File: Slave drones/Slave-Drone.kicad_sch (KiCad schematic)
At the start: 41 parts, among them J1 Conn_01x02, J2 Conn_01x02, J3 Conn_01x02, J4 Conn_01x02, J5 USB_C_Receptacle_USB2.0_16P, J6 Conn_01x02, SW1 SW_Push, SW2 SW_Push, U1 MPU6500, U2 QMC5883L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

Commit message: tried fixing error 3 - failed - use work around
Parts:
- U3: footprint ESP32-S3-MINI-1-N8:XCVR_ESP32-S3-MINI-1-N8 -> footprint-JLC:BULETM-SMD_ESP32-S3-MINI-1-N8
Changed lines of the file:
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@@
 			)
 		)
-		(property "Footprint" "ESP32-S3-MINI-1-N8:XCVR_ESP32-S3-MINI-1-N8"
+		(property "Footprint" "footprint-JLC:BULETM-SMD_ESP32-S3-MINI-1-N8"
 			(at 167.64 119.38 0)
 			(hide yes)

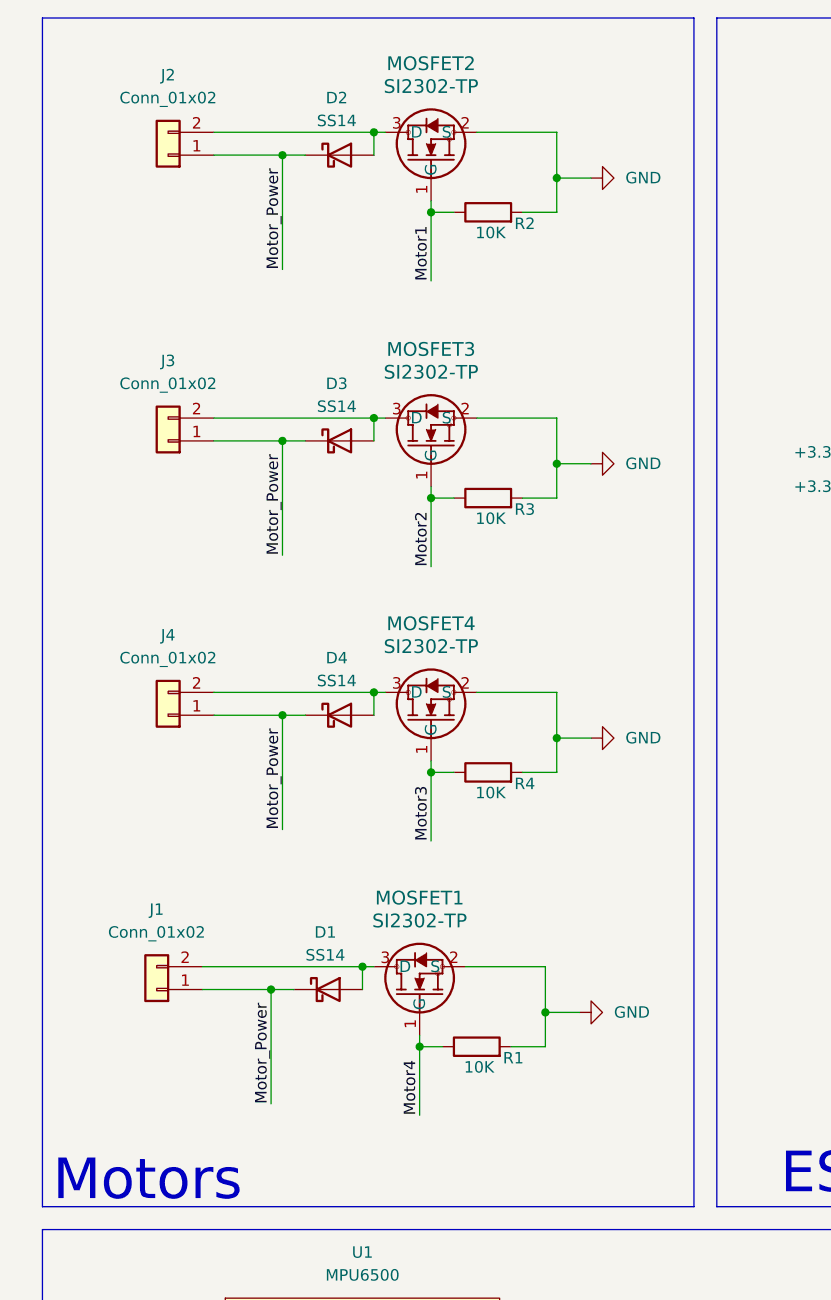
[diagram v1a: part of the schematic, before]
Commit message: corrected mosfet placement
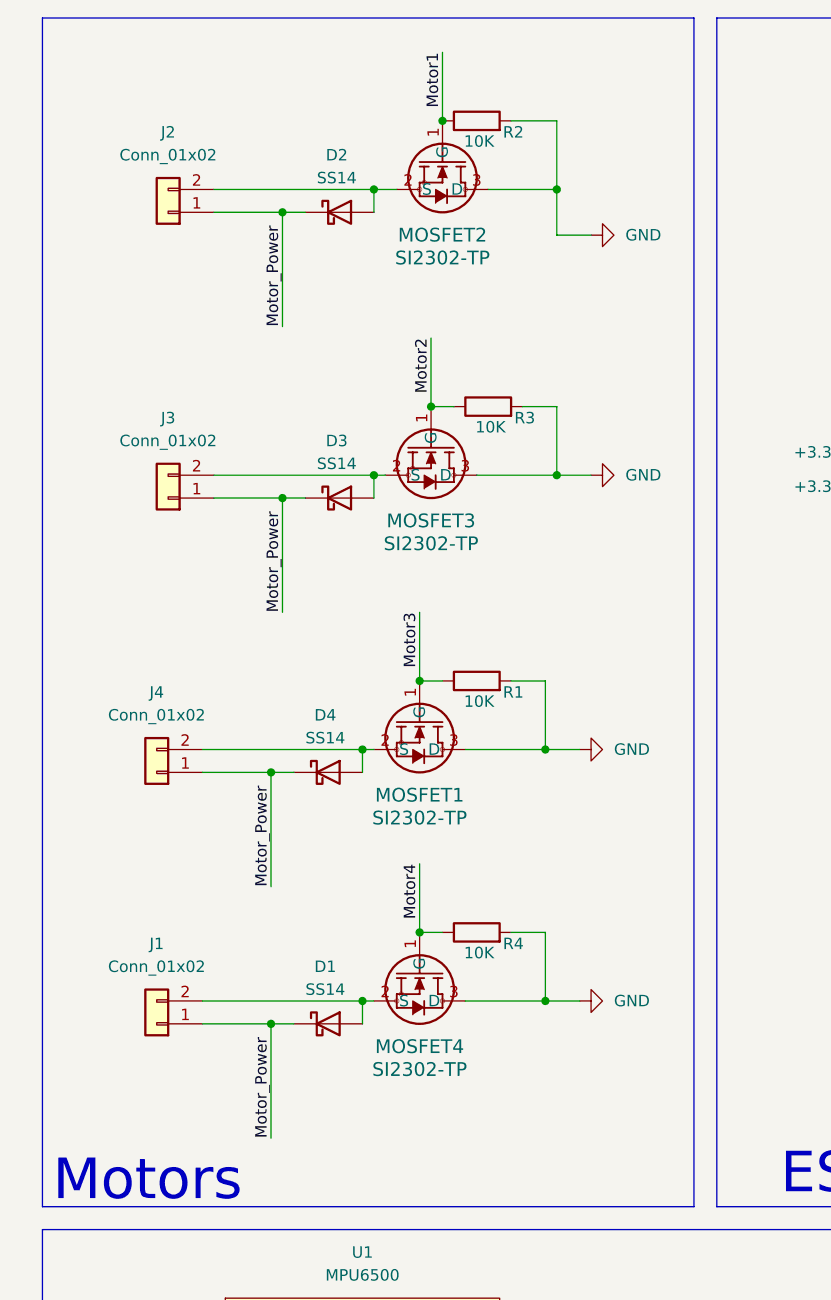
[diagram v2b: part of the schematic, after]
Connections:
- net GND: now also MOSFET1.3 (D), MOSFET2.3 (D), MOSFET3.3 (D), MOSFET4.3 (D); no longer MOSFET1.2 (S), MOSFET2.2 (S), MOSFET3.2 (S), MOSFET4.2 (S)
- net Motor3: now also MOSFET1.1 (G), R1.1; no longer MOSFET4.1 (G), R4.1
- net Motor4: now also MOSFET4.1 (G), R4.1; no longer MOSFET1.1 (G), R1.1
- net at D1.2 (A), J1.2 (Pin_2): now also MOSFET4.2 (S); no longer MOSFET1.3 (D)
- net at D2.2 (A), J2.2 (Pin_2): now also MOSFET2.2 (S); no longer MOSFET2.3 (D)
- net at D3.2 (A), J3.2 (Pin_2): now also MOSFET3.2 (S); no longer MOSFET3.3 (D)
- net at D4.2 (A), J4.2 (Pin_2): now also MOSFET1.2 (S); no longer MOSFET4.3 (D)
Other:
- moved on the sheet: D2, D3, J1, J2, J3, J4, MOSFET2, MOSFET3, R2, R3

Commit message: nothing
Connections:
- net GND: now also MOSFET1.2 (S), MOSFET2.2 (S), MOSFET3.2 (S), MOSFET4.2 (S); no longer MOSFET1.3 (D), MOSFET2.3 (D), MOSFET3.3 (D), MOSFET4.3 (D)
- net Motor3: now also MOSFET4.1 (G), R4.1; no longer MOSFET1.1 (G), R1.1
- net Motor4: now also MOSFET1.1 (G), R1.1; no longer MOSFET4.1 (G), R4.1
- net at D4.2 (A), J4.2 (Pin_2): now also MOSFET4.3 (D); no longer MOSFET1.2 (S)
- net at D2.2 (A), J2.2 (Pin_2): now also MOSFET2.3 (D); no longer MOSFET2.2 (S)
- net at D3.2 (A), J3.2 (Pin_2): now also MOSFET3.3 (D); no longer MOSFET3.2 (S)
- net at D1.2 (A), J1.2 (Pin_2): now also MOSFET1.3 (D); no longer MOSFET4.2 (S)
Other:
- moved on the sheet: D2, D3, J1, J2, J3, J4, MOSFET2, MOSFET3, R2, R3
